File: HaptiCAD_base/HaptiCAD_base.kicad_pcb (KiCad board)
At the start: 4 copper layers, 170 x 110 mm, 52 parts, among them J301 USB_C_Receptacle_USB2.0_16P, U201 SN74LV1T34DBV, U402 VEML7700-TT, U501 AP2112K-3.3

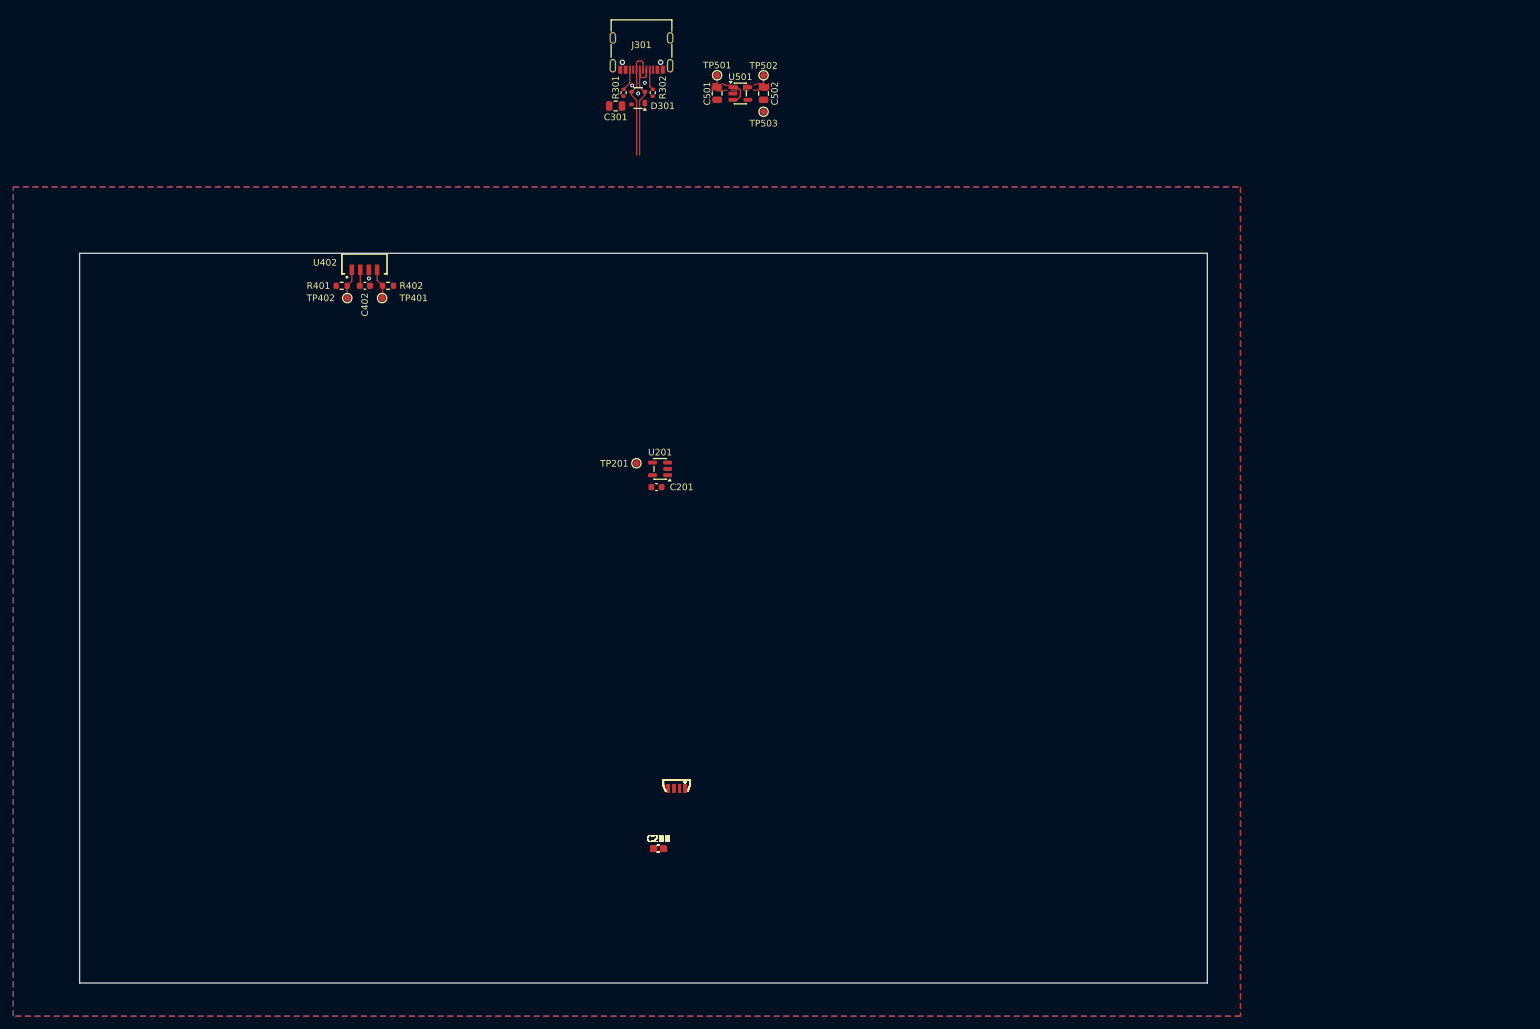
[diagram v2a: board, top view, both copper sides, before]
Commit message: Finished the layout for the base and motor mount
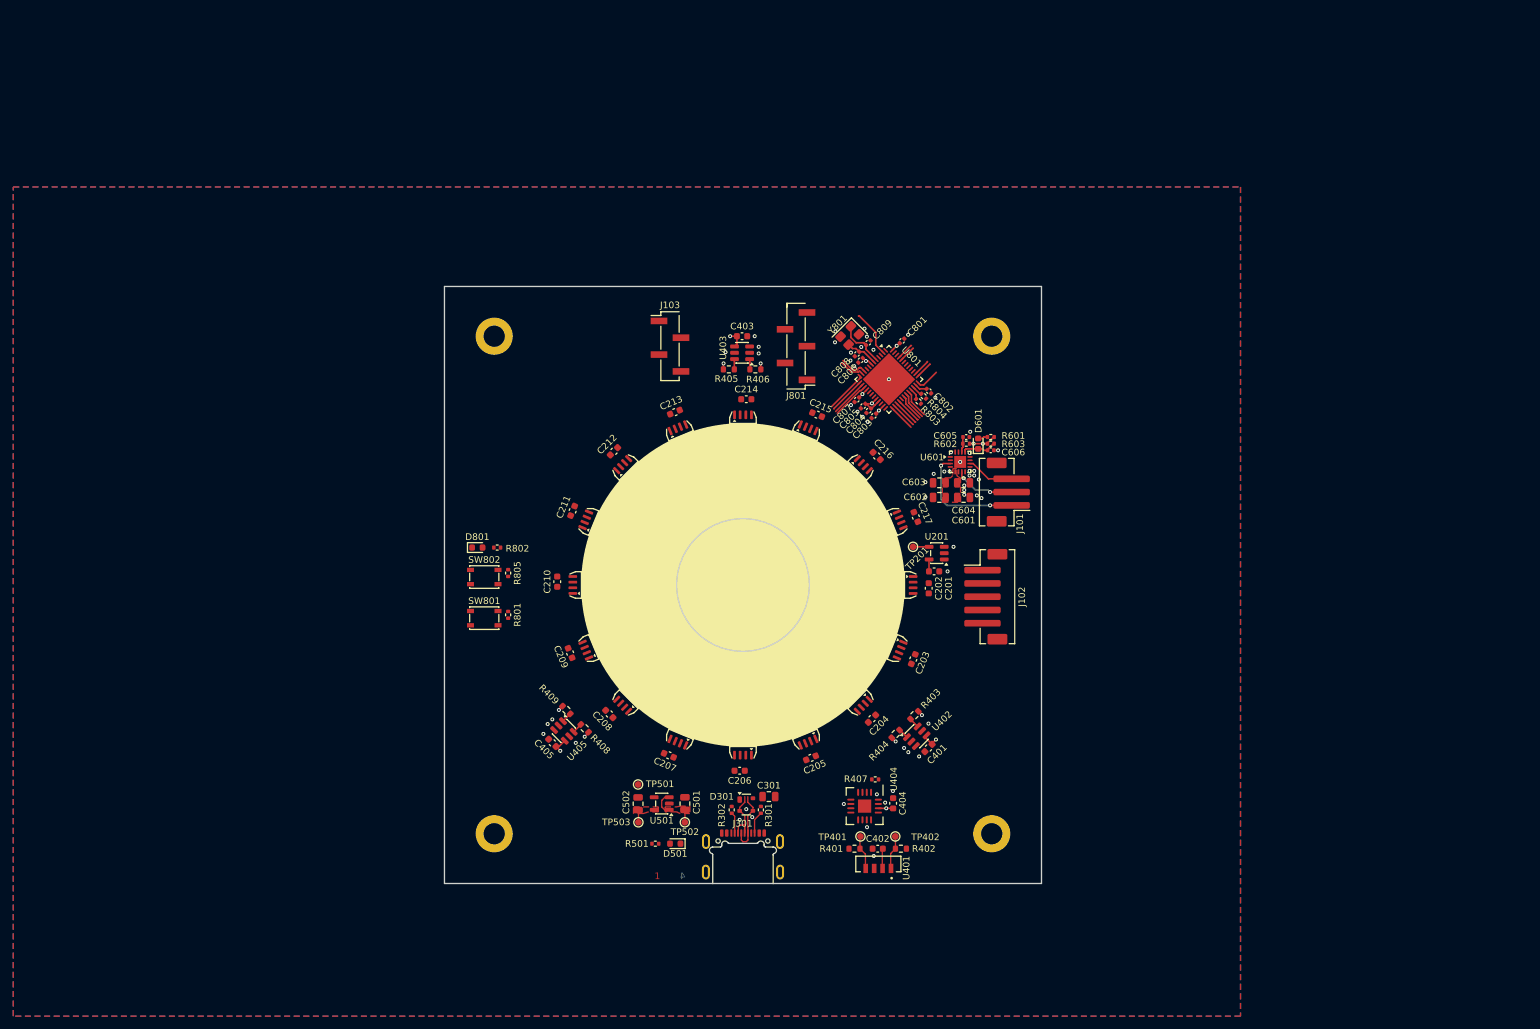
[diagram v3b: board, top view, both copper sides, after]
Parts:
- removed the C217 at (137.2, 139.8)
- removed the LED216 at (140.0, 130.0)
- removed LED217: WS2812_4020, PCM_marbastlib-xp-various:LED_WS2812_4020
- added C202: 0.1uF, Capacitor_SMD:C_0603_1608Metric, F.Cu at (178.0, 100.5)
- added C401: 0.1uF, Capacitor_SMD:C_0603_1608Metric, F.Cu at (178.0, 124.6)
- added C403: 0.1uF, Capacitor_SMD:C_0603_1608Metric, F.Cu at (149.9, 62.5)
- added C404: 0.1uF, Capacitor_SMD:C_0603_1608Metric, F.Cu at (172.6, 132.9)
- added C405: 0.1uF, Capacitor_SMD:C_0603_1608Metric, F.Cu at (121.3, 123.8)
- added C601: 22uF, Capacitor_SMD:C_0805_2012Metric, F.Cu at (183.3, 86.8)
- added C602: 22uF, Capacitor_SMD:C_0805_2012Metric, F.Cu at (179.6, 86.8)
- added C603: 2.2uF, Capacitor_SMD:C_0805_2012Metric, F.Cu at (179.6, 84.6)
- added C604: 2.2uF, Capacitor_SMD:C_0805_2012Metric, F.Cu at (183.2, 84.6)
- added C605: 1nF, Capacitor_SMD:C_0402_1005Metric, F.Cu at (183.7, 77.7)
- added C606: 10nF, Capacitor_SMD:C_0402_1005Metric, F.Cu at (187.3, 79.7)
- added C801: 0.1uF, Capacitor_SMD:C_0402_1005Metric, F.Cu at (174.0, 63.2)
- added C802: 0.1uF, Capacitor_SMD:C_0402_1005Metric, F.Cu at (178.0, 70.8)
- added C803: 0.1uF, Capacitor_SMD:C_0402_1005Metric, F.Cu at (169.7, 74.5)
- added C804: 0.1uF, Capacitor_SMD:C_0402_1005Metric, F.Cu at (168.9, 73.7)
- added C805: 0.1uF, Capacitor_SMD:C_0402_1005Metric, F.Cu at (168.1, 73.0)
- added C806: 0.1uF, Capacitor_SMD:C_0402_1005Metric, F.Cu at (167.7, 66.1)
- added C807: 0.1uF, Capacitor_SMD:C_0402_1005Metric, F.Cu at (167.2, 72.1)
- added C808: 20pF, Capacitor_SMD:C_0402_1005Metric, F.Cu at (167.2, 65.2)
- added C809: 20pF, Capacitor_SMD:C_0402_1005Metric, F.Cu at (168.9, 63.5)
- added D501: VPWR, Diode_SMD:D_0603_1608Metric, F.Cu at (139.8, 139.0)
- added D601: FAULT, Diode_SMD:D_0603_1608Metric, F.Cu at (185.5, 78.7)
- added D801: USER, Diode_SMD:D_0603_1608Metric, F.Cu at (110.0, 94.4)
- added H101: MountingHole_Pad, MountingHole:MountingHole_3.2mm_M3_DIN965_Pad, F.Cu at (112.5, 62.5)
- added H102: MountingHole_Pad, MountingHole:MountingHole_3.2mm_M3_DIN965_Pad, F.Cu at (187.5, 62.5)
- added H103: MountingHole_Pad, MountingHole:MountingHole_3.2mm_M3_DIN965_Pad, F.Cu at (112.5, 137.5)
- added H104: MountingHole_Pad, MountingHole:MountingHole_3.2mm_M3_DIN965_Pad, F.Cu at (187.5, 137.5)
- added J101: BLDC, Connector_JST:JST_PH_B3B-PH-SM4-TB_1x03-1MP_P2.00mm_Vertical, F.Cu at (190.0, 86.0)
- added J102: ENC, Connector_JST:JST_PH_B5B-PH-SM4-TB_1x05-1MP_P2.00mm_Vertical, F.Cu at (186.6, 101.8)
- added J103: EXT_UART, Connector_PinHeader_2.54mm:PinHeader_1x04_P2.54mm_Vertical_SMD_Pin1Left, F.Cu at (139.0, 64.0)
- added J801: SWD, Connector_PinHeader_2.54mm:PinHeader_1x05_P2.54mm_Vertical_SMD_Pin1Left, F.Cu at (158.0, 64.0)
- added LED201: WS2812_4020, PCM_marbastlib-xp-various:LED_WS2812_4020, F.Cu at (175.0, 100.0)
- added LED202: WS2812_4020, PCM_marbastlib-xp-various:LED_WS2812_4020, F.Cu at (173.1, 109.6)
- added R402: 2.2k, Resistor_SMD:R_0603_1608Metric, F.Cu at (173.8, 139.8)
- added R404: 2.2k, Resistor_SMD:R_0603_1608Metric, F.Cu at (173.0, 122.5)
- added R405: 2.2k, Resistor_SMD:R_0603_1608Metric, F.Cu at (147.9, 67.5)
- added R406: 2.2k, Resistor_SMD:R_0603_1608Metric, F.Cu at (151.9, 67.5)
- added R407: 10k, Resistor_SMD:R_0402_1005Metric, F.Cu at (169.9, 129.3)
- added R408: 2.2k, Resistor_SMD:R_0603_1608Metric, F.Cu at (126.1, 121.6)
- added R409: 2.2k, Resistor_SMD:R_0603_1608Metric, F.Cu at (123.4, 118.8)
- added R501: 5.1k, Resistor_SMD:R_0402_1005Metric, F.Cu at (136.8, 139.0)
- added R601: 3.3k, Resistor_SMD:R_0402_1005Metric, F.Cu at (187.4, 77.7)
- added R602: 18k, Resistor_SMD:R_0402_1005Metric, F.Cu at (183.7, 78.7)
- added R603: 18k, Resistor_SMD:R_0402_1005Metric, F.Cu at (187.4, 78.7)
- added R801: 10k, Resistor_SMD:R_0402_1005Metric, F.Cu at (114.6, 104.5)
- added R802: 5.1k, Resistor_SMD:R_0402_1005Metric, F.Cu at (113.0, 94.4)
- added R803: 27, Resistor_SMD:R_0402_1005Metric, F.Cu at (176.5, 72.3)
- added R804: 27, Resistor_SMD:R_0402_1005Metric, F.Cu at (177.2, 71.5)
- added R805: 10k, Resistor_SMD:R_0402_1005Metric, F.Cu at (114.6, 98.2)
- added S101: Layer marker, Symbol:LayerMarker_4_6.35x2.54mm_TextH1mm_P1.27mm_BottomMirrored, F.Cu at (137.1, 145.1)
- added SW801: SW_Push, Button_Switch_SMD:SW_SPST_PTS810, F.Cu at (111.0, 105.0)
- added SW802: SW_Push, Button_Switch_SMD:SW_SPST_PTS810, F.Cu at (111.0, 98.8)
- added U401: VEML7700-TR, VEML7700-TR:XDCR_VEML7700-TR, F.Cu at (170.4, 142.1)
- added U403: TLV493D, Package_TO_SOT_SMD:SOT-23-6, F.Cu at (149.9, 65.0)
- added U404: PCA9546A, PCA9546A:QFN-16_EP_5.25x5.25_Pitch0.65mm, F.Cu at (168.3, 133.3)
- added U405: TLV493D, Package_TO_SOT_SMD:SOT-23-6, F.Cu at (123.0, 122.0)
- added U601: STSPIN233, Package_DFN_QFN:VQFN-16-1EP_3x3mm_P0.5mm_EP1.8x1.8mm, F.Cu at (182.7, 81.5)
- added U801: STM32G431CBUx, Package_DFN_QFN:QFN-48-1EP_7x7mm_P0.5mm_EP5.6x5.6mm, F.Cu at (172.0, 69.0)
- added Y801: 12MHz, Crystal:Crystal_SMD_3225-4Pin_3.2x2.5mm, F.Cu at (166.1, 62.4)
- C301: value 100nF -> 0.1uF
- J301: footprint Connector_USB:USB_C_Receptacle_G-Switch_GT-USB-7010ASV -> PCM_marbastlib-various:USB_C_Receptacle_HRO_TYPE-C-31-M-14
- TP501: value 5V -> GND
- TP502: value 3.3V -> +5V
- TP503: value GND -> 3.3V
- U402: value VEML7700-TT -> TLV493D; footprint PCM_SparkFun-Sensor:VEML7700-TT -> Package_TO_SOT_SMD:SOT-23-6
- moved J301 121.0 mm to (150.0, 138.6), turned to 0 degrees
- moved TP402 115.8 mm to (173.0, 137.9), turned to 180 degrees
- moved C402 114.8 mm to (170.3, 139.8), turned to 180 degrees
- moved TP502 113.2 mm to (141.2, 135.8), turned to 180 degrees
- moved R401 110.2 mm to (166.8, 139.8), turned to 180 degrees
- moved R301 110.1 mm to (152.7, 133.9), turned to -90 degrees
- moved U402 109.6 mm to (176.2, 122.8), turned to 45 degrees
- moved TP503 108.8 mm to (134.2, 135.8), turned to 180 degrees
- moved R302 108.8 mm to (148.3, 133.9), turned to -90 degrees
- moved C502 108.7 mm to (134.2, 133.0), turned to 90 degrees
- moved TP401 108.6 mm to (167.7, 137.9), turned to 180 degrees
- moved R403 107.9 mm to (175.8, 119.6), turned to 45 degrees
- moved D301 107.7 mm to (150.5, 133.1), turned to 0 degrees
- moved U501 107.7 mm to (137.7, 132.9), turned to 180 degrees
- moved TP501 107.6 mm to (134.2, 130.1), turned to 90 degrees
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- renumbered C202 to C217, LED202 to LED216, R402 to R401, R401 to R403
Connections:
- C201 pad 1: 5V -> +5V
- C203 pad 1: 5V -> +5V
- C204 pad 1: 5V -> +5V
- C205 pad 1: 5V -> +5V
- C206 pad 1: 5V -> +5V
- C207 pad 1: 5V -> +5V
- C208 pad 1: 5V -> +5V
- C209 pad 1: 5V -> +5V
- C210 pad 1: 5V -> +5V
- C211 pad 1: 5V -> +5V
- C212 pad 1: 5V -> +5V
- C213 pad 1: 5V -> +5V
- C214 pad 1: 5V -> +5V
- C215 pad 1: 5V -> +5V
- C216 pad 1: 5V -> +5V
- C217 pad 1: 5V -> +5V
- C301 pad 1: 5V -> +5V
- C402 pad 1: 3.3V -> +3V3
- C501 pad 1: 5V -> +5V
- C502 pad 1: 3.3V -> +3V3
- D301 pad 4: 5V -> +5V
- J301 pad A4: 5V -> +5V
- J301 pad A9: 5V -> +5V
- J301 pad B4: 5V -> +5V
- J301 pad B9: 5V -> +5V
- LED203 pad 2: 5V -> +5V
- LED204 pad 2: 5V -> +5V
- LED205 pad 2: 5V -> +5V
- LED206 pad 2: 5V -> +5V
- LED207 pad 2: 5V -> +5V
- LED208 pad 2: 5V -> +5V
- LED209 pad 2: 5V -> +5V
- LED210 pad 1: Net-(LED210-DIN) -> Net-(LED209-DOUT)
- LED210 pad 2: 5V -> +5V
- LED210 pad 3: unconnected-(LED210-DOUT-Pad3) -> Net-(LED210-DOUT)
- LED211 pad 1: Net-(LED211-DIN) -> Net-(LED210-DOUT)
- LED211 pad 2: 5V -> +5V
- LED211 pad 3: Net-(LED210-DIN) -> Net-(LED211-DOUT)
- LED212 pad 1: Net-(LED212-DIN) -> Net-(LED211-DOUT)
- LED212 pad 2: 5V -> +5V
- LED212 pad 3: Net-(LED211-DIN) -> Net-(LED212-DOUT)
- LED213 pad 1: Net-(LED213-DIN) -> Net-(LED212-DOUT)
- LED213 pad 2: 5V -> +5V
- LED213 pad 3: Net-(LED212-DIN) -> Net-(LED213-DOUT)
- LED214 pad 1: Net-(LED214-DIN) -> Net-(LED213-DOUT)
- LED214 pad 2: 5V -> +5V
- LED214 pad 3: Net-(LED213-DIN) -> Net-(LED214-DOUT)
- LED215 pad 1: Net-(LED215-DIN) -> Net-(LED214-DOUT)
- LED215 pad 2: 5V -> +5V
- LED215 pad 3: Net-(LED214-DIN) -> Net-(LED215-DOUT)
- LED216 pad 1: Net-(LED202-DIN) -> Net-(LED215-DOUT)
- LED216 pad 2: 5V -> +5V
- LED216 pad 3: Net-(LED202-DOUT) -> unconnected-(LED216-DOUT-Pad3)
- R401 pad 1: /MCU/I2C1_SDA -> /MCU/I2C1_SCL
- R401 pad 2: 3.3V -> +3V3
- R403 pad 1: /MCU/I2C1_SCL -> /Sensors/SCL0
- R403 pad 2: 3.3V -> +3V3
- TP201 pad 1: Net-(LED202-DIN) -> Net-(LED201-DIN)
- TP501 pad 1: 5V -> GND
- TP502 pad 1: 3.3V -> +5V
- TP503 pad 1: GND -> +3V3
- U201 pad 4: Net-(LED202-DIN) -> Net-(LED201-DIN)
- U201 pad 5: 5V -> +5V
- U402 pad 1: /MCU/I2C1_SCL -> /Sensors/SDA0
- U402 pad 2: 3.3V -> GND
- U402 pad 4: /MCU/I2C1_SDA -> +3V3
- U501 pad 1: 5V -> +5V
- U501 pad 3: 5V -> +5V
- U501 pad 5: 3.3V -> +3V3
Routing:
- net +3V3: track 0.00 -> 33.4 mm, vias 0 -> 15
- net /Motor driver/MOT_U: track 0.00 -> 17.7 mm, vias 0 -> 2
- net /Motor driver/MOT_V: track 0.00 -> 9.19 mm, vias 0 -> 2
- net /MCU/USB_D-: track 16.6 -> 9.22 mm
- net /MCU/USB_D+: track 16.9 -> 9.50 mm
- net /MCU/XOUT: track 0.00 -> 7.29 mm
- net +5V: track 0.00 -> 7.24 mm
- net /Motor driver/MOT_W: track 0.00 -> 7.23 mm
- net /LED lighting/LED_DATA: track 0.00 -> 7.16 mm
- net /MCU/~{ENC_CS}: track 0.00 -> 6.35 mm
- net /MCU/~{MOT_SHDN}: track 0.00 -> 6.23 mm
- net /MCU/USR_LED: track 0.00 -> 5.72 mm
- net /MCU/SPI1_CIPO: track 0.00 -> 5.66 mm
- net /MCU/SPI1_SCK: track 0.00 -> 5.58 mm
- net 5V: track 5.43 -> 0.00 mm
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- added copper zone on F.Cu, net +3V3
- added copper zone on F.Cu, net +5V
- removed copper zone on F.Cu, net 3.3V
- removed copper zone on F.Cu, net 5V
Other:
- board size 170 x 110 mm -> 90 x 90 mm

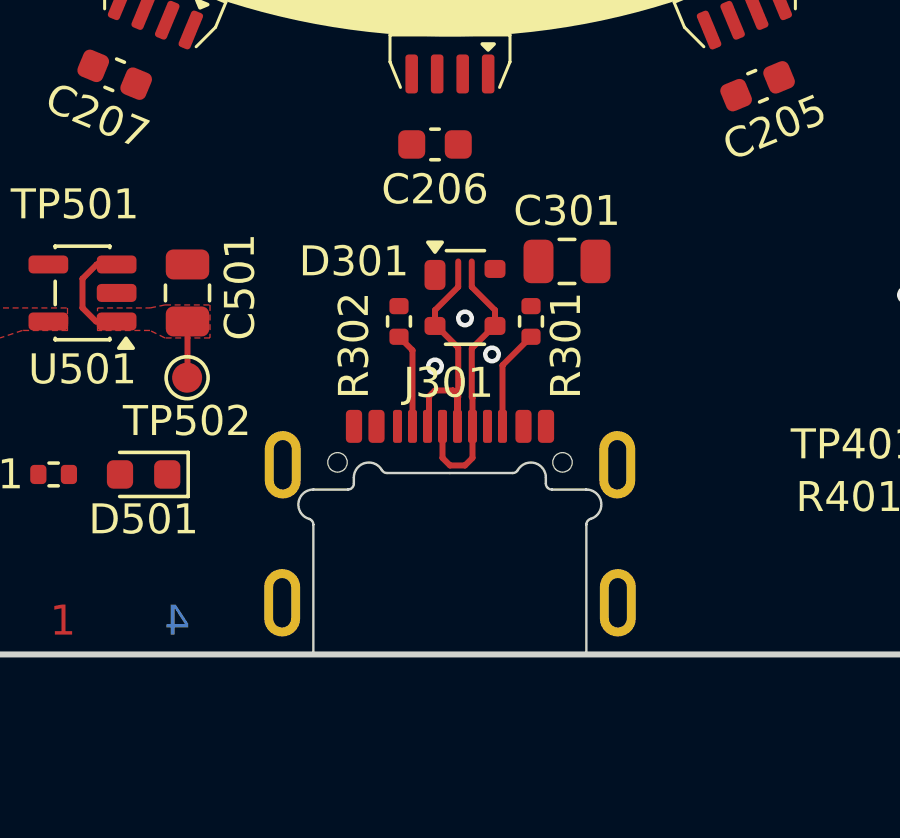
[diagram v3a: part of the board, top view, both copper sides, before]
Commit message: Added preliminary PCB CAD exports
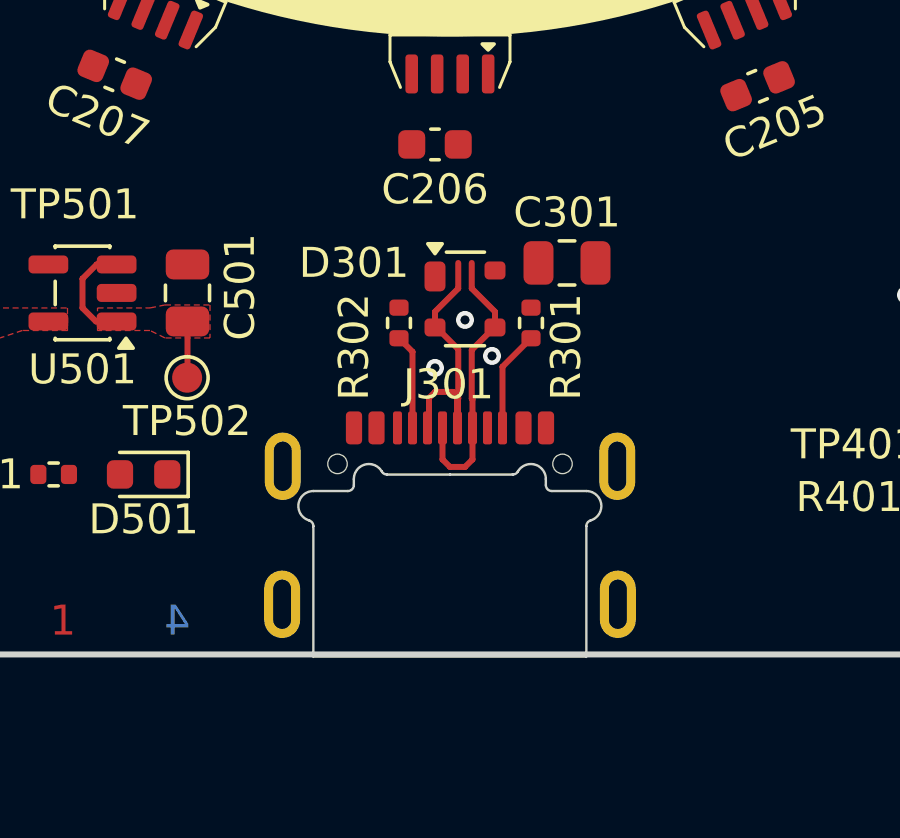
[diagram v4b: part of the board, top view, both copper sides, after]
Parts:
- moved C301 0.05 mm to (153.9, 132.0)
- moved D301 0.05 mm to (150.5, 133.2)
- moved J301 0.05 mm to (150.0, 138.6)
